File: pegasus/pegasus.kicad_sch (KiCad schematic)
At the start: 10 parts, among them IC1 RFD900, IC2 Adafruit_MPL3115A2, IC3 Adafruit-BNO055-PCB, IC4 L70B-M39, IC5 L7805ACV, J1 Conn_01x02_Female, J2 Conn_01x02_Female, U1 Teensy4.1, U2 CON-SMA-EDGE-S, U3 CON-SMA-EDGE-S

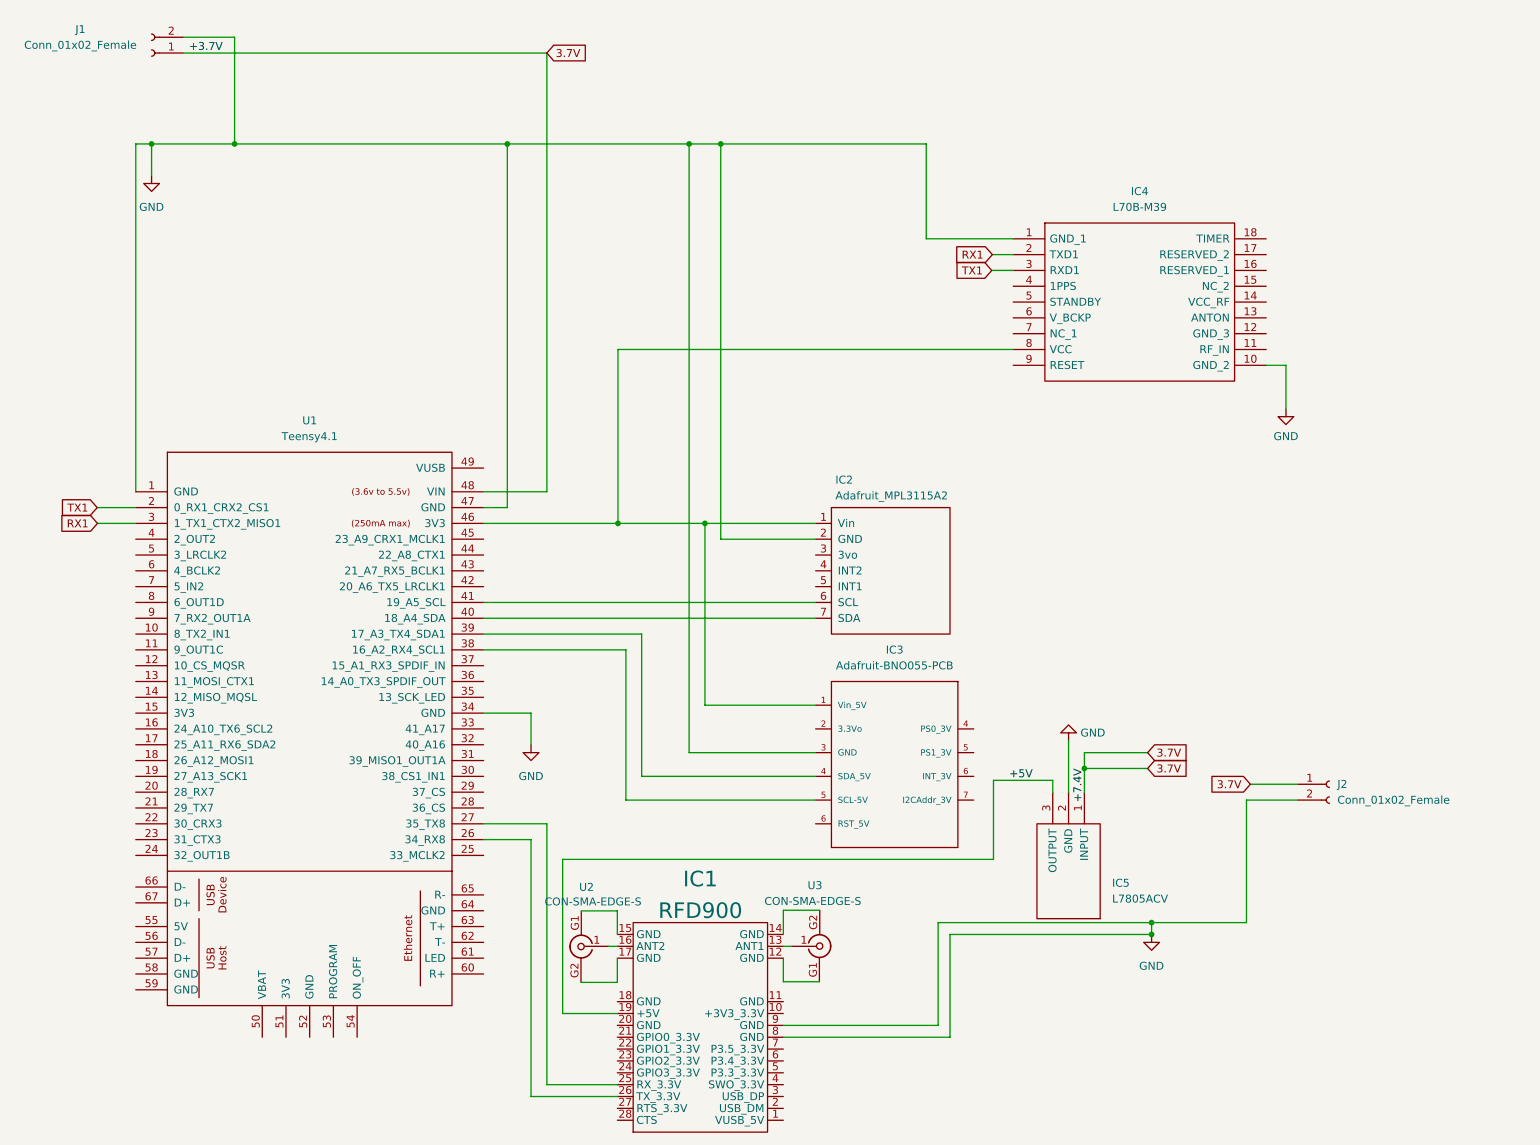
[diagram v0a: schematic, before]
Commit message: finalized board dimensions (50x120mm) and component positioning. completed draft of traces
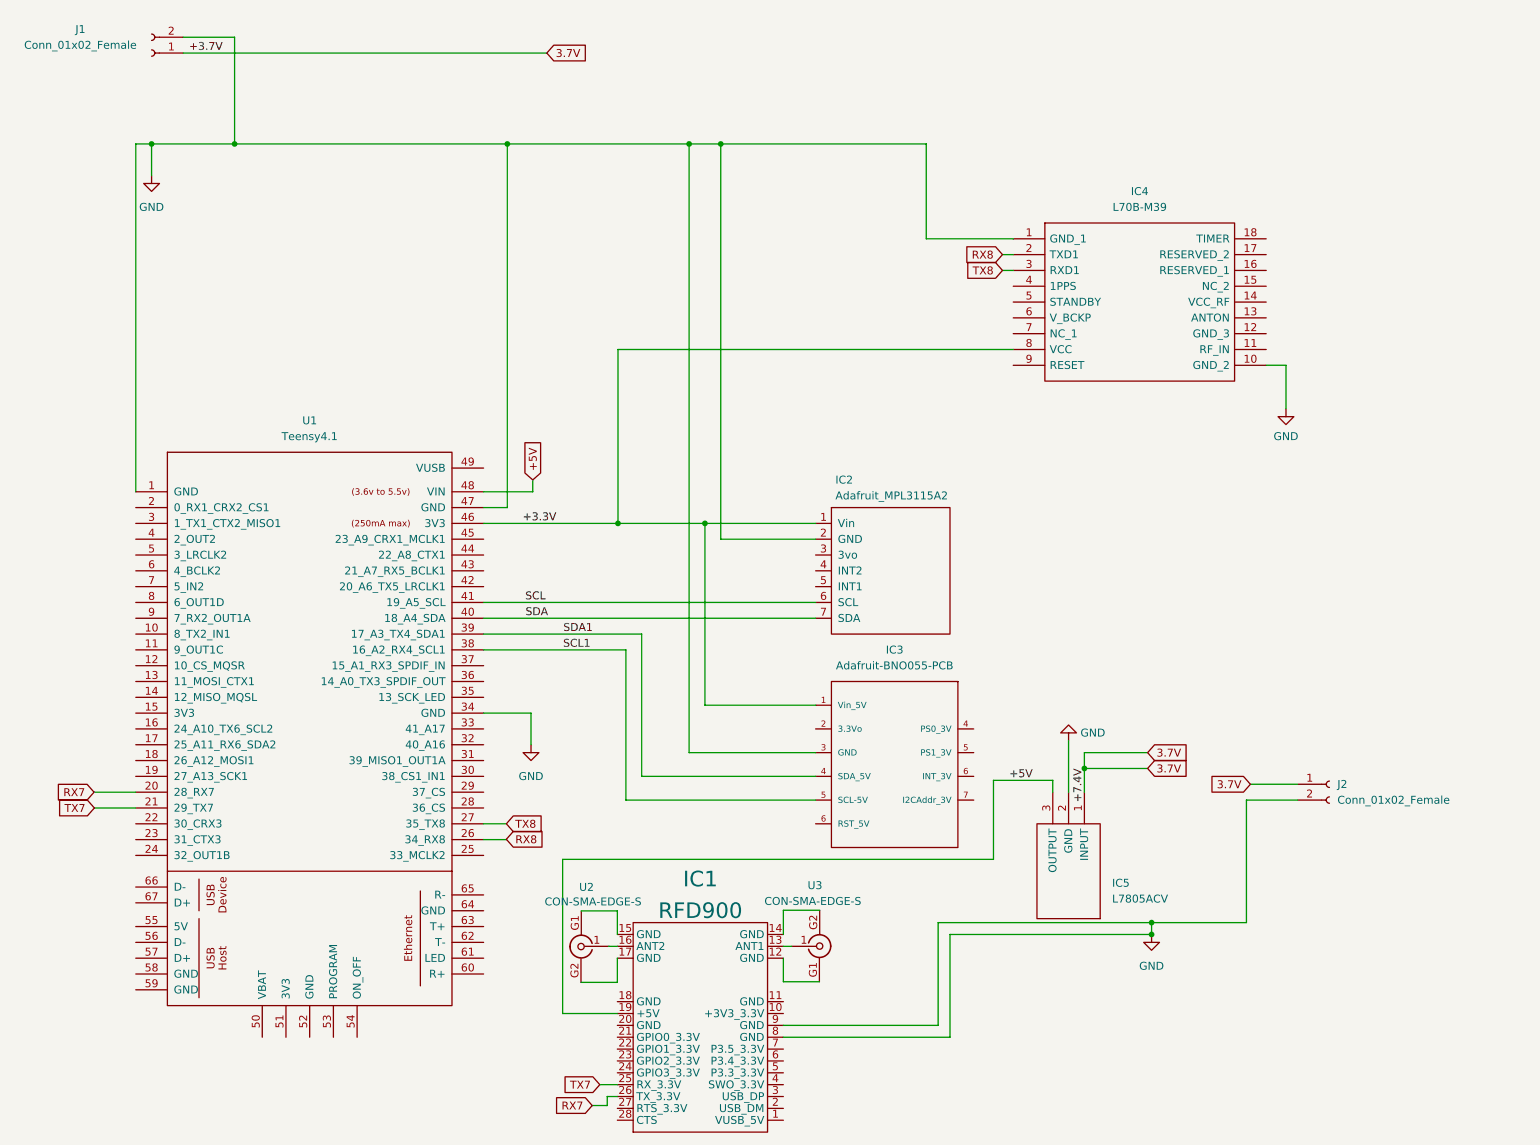
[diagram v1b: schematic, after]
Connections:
- net +5V: now also U1.48 (VIN)
- net 3.7V: no longer U1.48 (VIN)
- net RX7: now reaches U1.20 (28_RX7)
- net RX7: now also IC1.26 (TX_3.3V)
- net TX7: now reaches U1.21 (29_TX7)
- net TX7: now also IC1.25 (RX_3.3V)
- net RX8: now reaches U1.26 (34_RX8)
- net RX8: now also IC4.2 (TXD1); no longer IC1.26 (TX_3.3V)
- net TX8: now reaches U1.27 (35_TX8)
- net TX8: now also IC4.3 (RXD1); no longer IC1.25 (RX_3.3V)
- net SCL1: now reaches IC3.5 (SCL-5V), U1.38 (16_A2_RX4_SCL1)
- net SDA1: now reaches IC3.4 (SDA_5V), U1.39 (17_A3_TX4_SDA1)
- net SDA: now reaches IC2.7 (SDA), U1.40 (18_A4_SDA)
- net SCL: now reaches IC2.6 (SCL), U1.41 (19_A5_SCL)
- net +3.3V: now reaches IC2.1 (Vin), IC3.1 (Vin_5V), IC4.8 (VCC), U1.46 (3V3)
- net RX1: no longer names the net of U1.3 (1_TX1_CTX2_MISO1)
- net RX1: no longer IC4.2 (TXD1)
- net TX1: no longer names the net of U1.2 (0_RX1_CRX2_CS1)
- net TX1: no longer IC4.3 (RXD1)

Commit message: removed a wire
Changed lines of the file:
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@@
   (junction (at 57.785 35.56) (diameter 0) (color 0 0 0 0)
   )
-  (wire (pts (xy 179.705 150.495) (xy 110.49 150.495))
+  (wire (pts (xy 110.49 150.495) (xy 179.705 150.495))
     (stroke (width 0) (type default) (color 0 0 0 0))
   )
